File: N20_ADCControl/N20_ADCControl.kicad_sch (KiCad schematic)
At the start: 35 parts

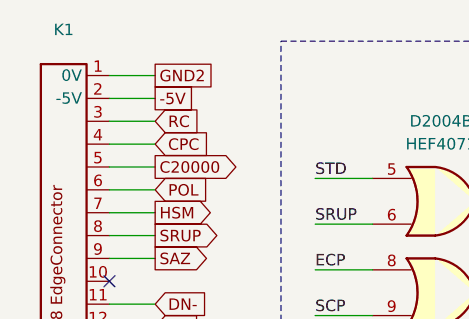
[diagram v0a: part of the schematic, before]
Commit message: Replaced testpins with testloops/beads
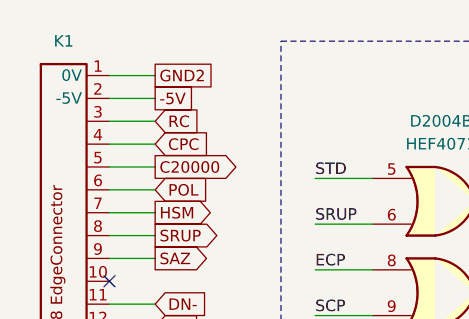
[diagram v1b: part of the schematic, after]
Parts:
- K1: symbol _PhilipsPM2528DMM:PCBEdge_Plugincard -> PM2528:PCBEdge_Plugincard
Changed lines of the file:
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@@
 	)
 	(symbol
-		(lib_id "_PhilipsPM2528DMM:PCBEdge_Plugincard")
+		(lib_id "PM2528:PCBEdge_Plugincard")
 		(at 17.78 41.91 0)
 		(unit 1)
@@
 		(fields_autoplaced yes)
 		(property "Reference" "K1"
-			(at 17.78 13.97 0)
+			(at 17.78 15.24 0)
 			(effects
 				(font

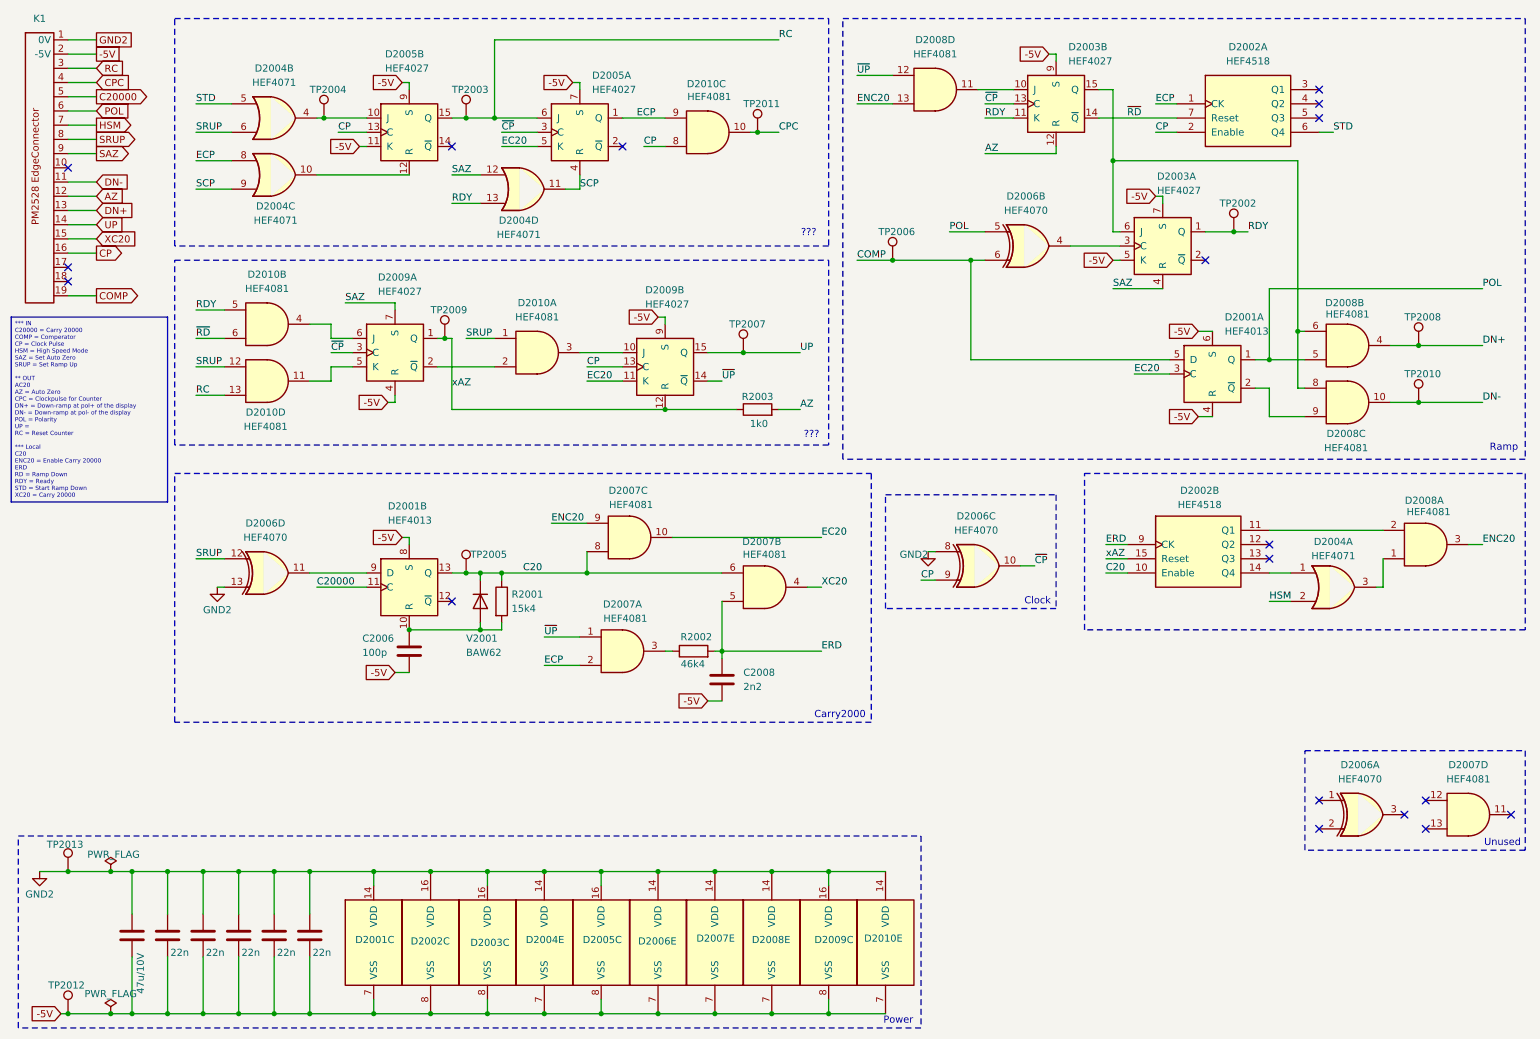
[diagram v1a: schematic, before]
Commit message: Added N22/N23
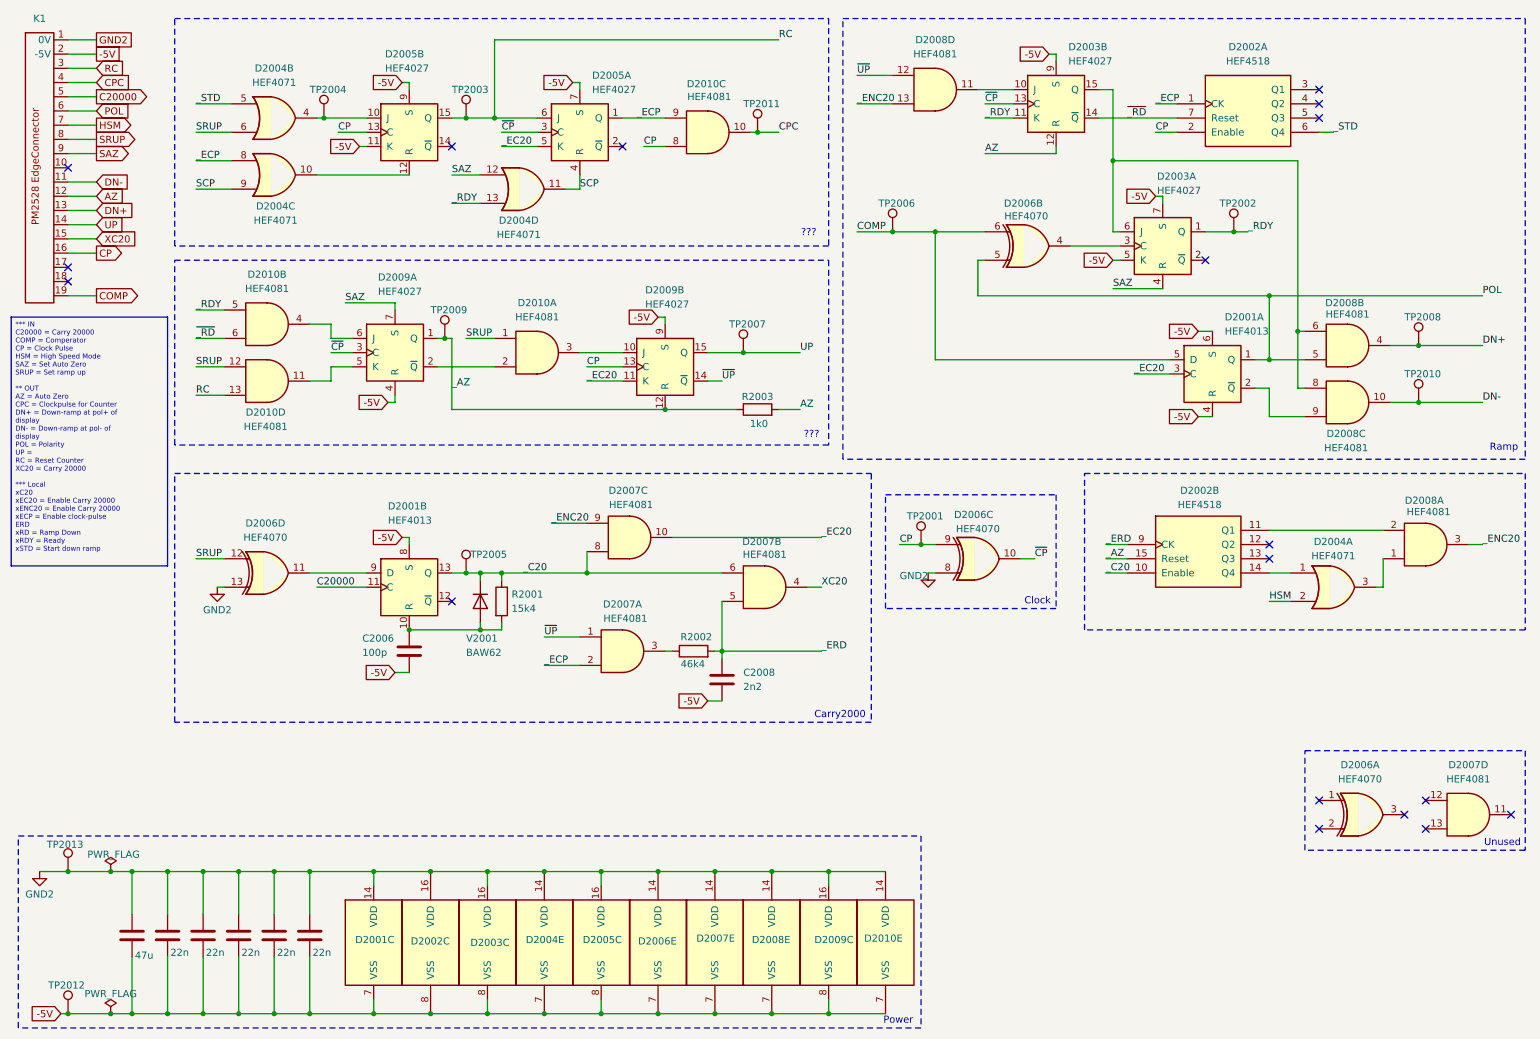
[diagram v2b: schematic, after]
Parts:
- added TP2001: TestPoint, Connector_PinHeader_1.00mm:PinHeader_1x01_P1.00mm_Vertical, symbol Connector:TestPoint
- C2007: value 47u/10V -> 47u
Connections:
- net CP: now also TP2001.1
- net C20 renamed _C20
- net EC20 renamed _EC20
- net ECP renamed _ECP
- net ENC20 renamed _ENC20
- net ERD renamed _ERD
- net RDY renamed _RDY
- net STD renamed _STD
- net xAZ renamed _AZ
- net ~{RD} renamed ~{_RD}
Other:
- moved on the sheet: D2006C, TP2006

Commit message: Updates, add N25
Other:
- note added: "Carry20000"
- note added: "Supply zero"
- note removed: "???"
- note removed: "Carry2000"
- title: PM2528 N20 (ADC Control) -> Philips PM2528 - N20 (ADC Control)
- moved on the sheet: C2006, C2008, D2001A, D2001B, D2001C, D2002A, D2002B, D2002C, D2003A, D2003B, D2003C, D2004A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
